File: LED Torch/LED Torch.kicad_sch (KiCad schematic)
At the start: 4 parts, among them SW1 SW_Push

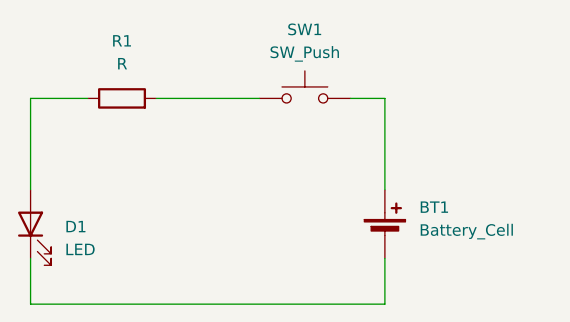
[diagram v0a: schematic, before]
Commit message: Battery deleted
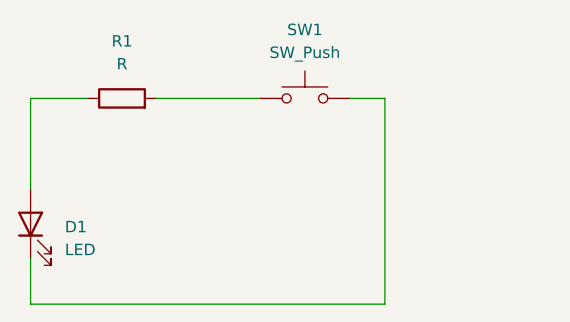
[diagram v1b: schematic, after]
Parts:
- removed BT1: Battery_Cell, symbol Device:Battery_Cell
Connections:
- net at D1.1 (K): now also SW1.2
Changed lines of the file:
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@@
-	(wire
-		(pts
-			(xy 154.94 99.06) (xy 154.94 104.14)
-		)
-		(stroke
-			(width 0)
-			(type default)
-		)
-	)
 	(wire
 		(pts
@@
 	(wire
 		(pts
-			(xy 154.94 81.28) (xy 154.94 91.44)
+			(xy 154.94 81.28) (xy 154.94 104.14)
 		)
 		(stroke
@@
 					(unit 1)
 				)
-			)
-		)
-	)
-	(symbol
-		(lib_id "Device:Battery_Cell")
-		(at 154.94 96.52 0)
-		(unit 1)
-		(exclude_from_sim no)
-		(in_bom yes)
-		(on_board yes)
-		(dnp no)
-		(fields_autoplaced yes)
-		(property "Reference" "BT1"
-			(at 158.75 93.4084 0)
-			(effects
-				(font
-					(size 1.27 1.27)
-				)
-				(justify left)
-			)
-		)
-		(property "Value" "Battery_Cell"
-			(at 158.75 95.9484 0)
-			(effects
-				(font
-					(size 1.27 1.27)
-				)
-				(justify left)
-			)
-		)
-		(property "Footprint" ""
-			(at 154.94 94.996 90)
-			(effects
-				(font
-					(size 1.27 1.27)
-				)
-				(hide yes)
-			)
-		)
-		(property "Datasheet" "~"
-			(at 154.94 94.996 90)
-			(effects
-				(font
-					(size 1.27 1.27)
-				)
-				(hide yes)
-			)
-		)
-		(property "Description" "Single-cell battery"
-			(at 154.94 96.52 0)
-			(effects
-				(font
-					(size 1.27 1.27)
-				)
-				(hide yes)
-			)
-		)
-		(pin "2"
-		)
-		(pin "1"
-		)
-		(instances
-			(project ""
-				(path "/448b5c88-0952-43dc-bbe6-98f9c5a72c71"
-					(reference "BT1")
-					(unit 1)
-				)
